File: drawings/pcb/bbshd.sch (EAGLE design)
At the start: 55 parts, among them IC1 LM358D

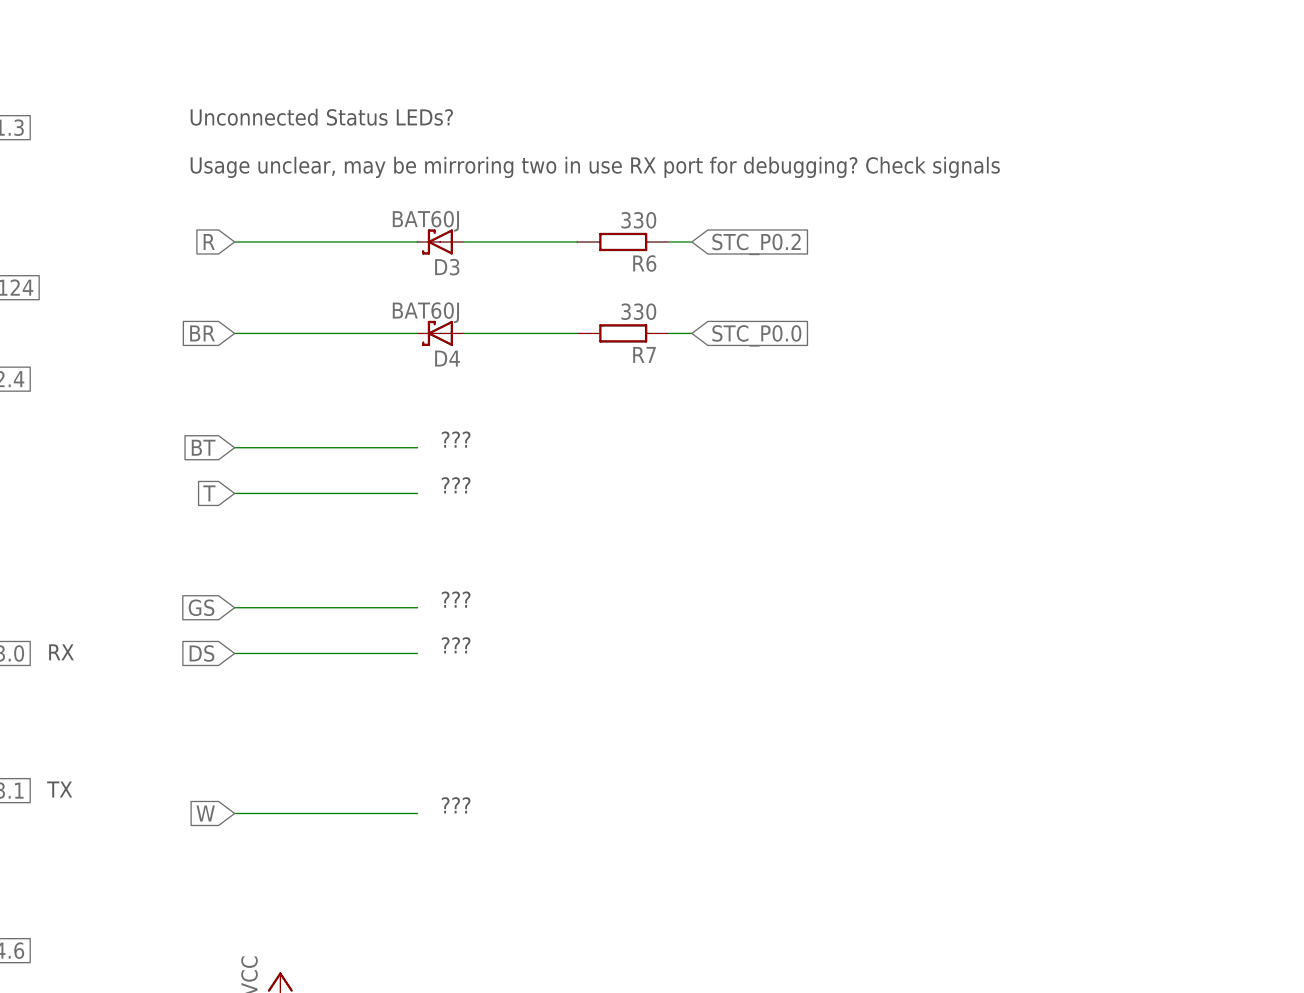
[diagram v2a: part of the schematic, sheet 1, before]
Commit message: Updated annotated photos with more info. Added info about additional UARTs brought out to pinheaders in schematic. Added template firmware src project, visual studio project files and makefile for SDCC compiler.
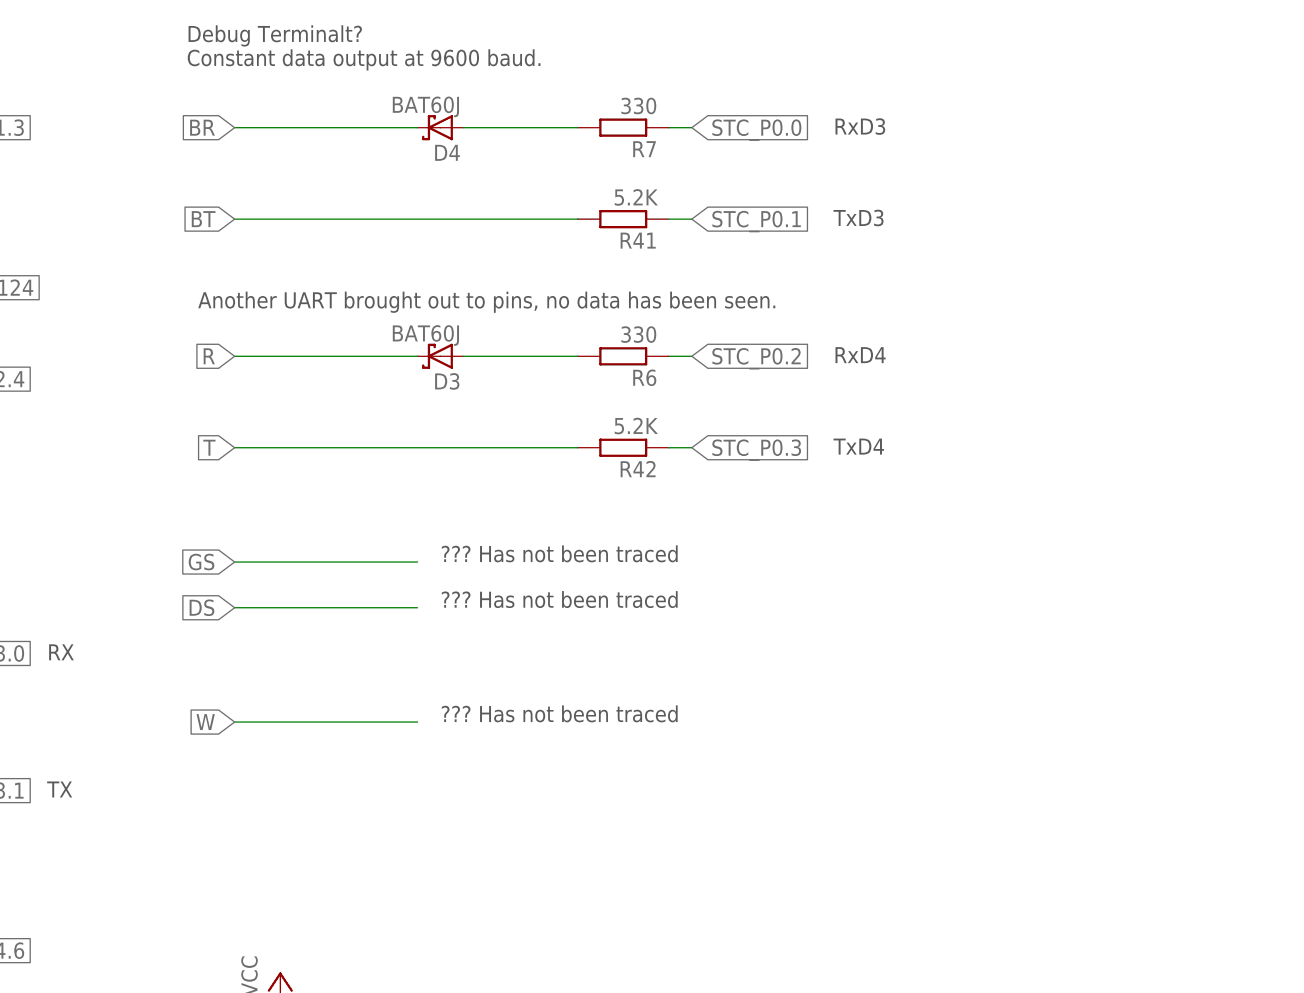
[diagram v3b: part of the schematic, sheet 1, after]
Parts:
- added R41, R42: 5.2K, rcl:R-EU_R0603
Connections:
- new net BT: R41.2
- new net STC_P0.1: R41.1
- new net STC_P0.3: R42.1
- new net T: R42.2
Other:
- note added: "??? Has not been traced"
- note added: "Another UART brought out to pins, no data has been seen."
- note added: "Debug Terminalt? Constant data output at 9600 baud."
- note added: "RxD3"
- note added: "RxD4"
- note added: "TxD3"
- note added: "TxD4"
- note removed: "???"
- note removed: "Unconnected Status LEDs? Usage unclear, may be mirroring two in use RX port for debugging? Check signals"
- moved on the sheet: D3, D4, R6, R7
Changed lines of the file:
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@@
 <part name="R40" library="rcl" deviceset="R-EU_" device="R0603" value="5.6K"/>
 <part name="LED1" library="led" deviceset="LED" device=""/>
+<part name="R41" library="rcl" deviceset="R-EU_" device="R0603" value="5.2K"/>
+<part name="R42" library="rcl" deviceset="R-EU_" device="R0603" value="5.2K"/>
 </parts>
 <sheets>
@@
 <text x="17.78" y="123.698" size="1.778" layer="97">GND</text>
 <text x="19.558" y="121.158" size="1.778" layer="97">5V</text>
-<text x="160.02" y="154.94" size="1.778" layer="97">Unconnected Status LEDs?
-Usage unclear, may be mirroring two in use RX port for debugging? Check signals</text>
 <text x="144.272" y="100.838" size="1.778" layer="97">RX</text>
 <text x="144.272" y="85.598" size="1.778" layer="97">TX</text>
@@
 <text x="17.018" y="60.198" size="1.778" layer="97">PAS1</text>
 <text x="17.018" y="62.738" size="1.778" layer="97">PAS2</text>
-<text x="187.96" y="124.46" size="1.778" layer="97">???</text>
-<text x="187.96" y="119.38" size="1.778" layer="97">???</text>
-<text x="187.96" y="106.68" size="1.778" layer="97">???</text>
-<text x="187.96" y="101.6" size="1.778" layer="97">???</text>
-<text x="187.96" y="83.82" size="1.778" layer="97">???</text>
+<text x="159.766" y="166.878" size="1.778" layer="97">Debug Terminalt?
+Constant data output at 9600 baud.</text>
+<text x="187.96" y="111.76" size="1.778" layer="97">??? Has not been traced</text>
+<text x="187.96" y="106.68" size="1.778" layer="97">??? Has not been traced</text>
+<text x="187.96" y="93.98" size="1.778" layer="97">??? Has not been traced</text>
 <text x="18.796" y="29.718" size="1.778" layer="97">SPD</text>
 <text x="217.17" y="20.066" size="2.54" layer="94">Daniel Nilsson</text>
 <text x="180.34" y="55.88" size="1.778" layer="97">ADC6 - Battery voltage measurement</text>
+<text x="231.648" y="123.698" size="1.778" layer="97">TxD4</text>
+<text x="231.648" y="133.858" size="1.778" layer="97">RxD4</text>
+<text x="231.648" y="159.258" size="1.778" layer="97">RxD3</text>
+<text x="231.648" y="149.098" size="1.778" layer="97">TxD3</text>
+<text x="161.036" y="139.954" size="1.778" layer="97">Another UART brought out to pins, no data has been seen.</text>
 </plain>
 <instances>
@@
 <instance part="P+3" gate="1" x="86.36" y="119.38"/>
 <instance part="D2" gate="G$1" x="78.74" y="101.6" rot="R180"/>
-<instance part="D3" gate="G$1" x="187.96" y="147.32" rot="R180"/>
-<instance part="R6" gate="G$1" x="208.28" y="147.32" rot="R180"/>
-<instance part="R7" gate="G$1" x="208.28" y="137.16" rot="R180"/>
-<instance part="D4" gate="G$1" x="187.96" y="137.16" rot="R180"/>
+<instance part="D3" gate="G$1" x="187.96" y="134.62" rot="R180"/>
+<instance part="R6" gate="G$1" x="208.28" y="134.62" rot="R180"/>
+<instance part="R7" gate="G$1" x="208.28" y="160.02" rot="R180"/>
+<instance part="D4" gate="G$1" x="187.96" y="160.02" rot="R180"/>
 <instance part="R8" gate="G$1" x="55.88" y="93.98" rot="R270"/>
 <instance part="D5" gate="G$1" x="55.88" y="109.22" rot="R270"/>
@@
 <instance part="R29" gate="G$1" x="182.88" y="48.26"/>
 <instance part="R30" gate="G$1" x="195.58" y="48.26"/>
+<instance part="R41" gate="G$1" x="208.28" y="149.86" rot="R180"/>
+<instance part="R42" gate="G$1" x="208.28" y="124.46" rot="R180"/>
 </instances>
 <busses>
@@
 <segment>
 <pinref part="D3" gate="G$1" pin="A"/>
-<wire x1="190.5" y1="147.32" x2="203.2" y2="147.32" width="0.1524" layer="91"/>
+<wire x1="190.5" y1="134.62" x2="203.2" y2="134.62" width="0.1524" layer="91"/>
 <pinref part="R6" gate="G$1" pin="2"/>
 </segment>
@@
 <segment>
 <pinref part="R6" gate="G$1" pin="1"/>
-<wire x1="213.36" y1="147.32" x2="215.9" y2="147.32" width="0.1524" layer="91"/>
-<label x="215.9" y="147.32" size="1.778" layer="95" xref="yes"/>
+<wire x1="213.36" y1="134.62" x2="215.9" y2="134.62" width="0.1524" layer="91"/>
+<label x="215.9" y="134.62" size="1.778" layer="95" xref="yes"/>
 </segment>
 </net>
@@
 <segment>
 <pinref part="R7" gate="G$1" pin="1"/>
-<wire x1="213.36" y1="137.16" x2="215.9" y2="137.16" width="0.1524" layer="91"/>
-<label x="215.9" y="137.16" size="1.778" layer="95" xref="yes"/>
+<wire x1="213.36" y1="160.02" x2="215.9" y2="160.02" width="0.1524" layer="91"/>
+<label x="215.9" y="160.02" size="1.778" layer="95" xref="yes"/>
 </segment>
 </net>
@@
 <pinref part="R7" gate="G$1" pin="2"/>
 <pinref part="D4" gate="G$1" pin="A"/>
-<wire x1="203.2" y1="137.16" x2="190.5" y2="137.16" width="0.1524" layer="91"/>
+<wire x1="203.2" y1="160.02" x2="190.5" y2="160.02" width="0.1524" layer="91"/>
 </segment>
 </net>
@@
 <segment>
 <pinref part="D3" gate="G$1" pin="C"/>
-<wire x1="185.42" y1="147.32" x2="165.1" y2="147.32" width="0.1524" layer="91"/>
-<label x="165.1" y="147.32" size="1.778" layer="95" rot="R180" xref="yes"/>
+<wire x1="185.42" y1="134.62" x2="165.1" y2="134.62" width="0.1524" layer="91"/>
+<label x="165.1" y="134.62" size="1.778" layer="95" rot="R180" xref="yes"/>
 </segment>
 </net>
@@
 <segment>
 <pinref part="D4" gate="G$1" pin="C"/>
-<wire x1="185.42" y1="137.16" x2="165.1" y2="137.16" width="0.1524" layer="91"/>
-<label x="165.1" y="137.16" size="1.778" layer="95" rot="R180" xref="yes"/>
+<wire x1="185.42" y1="160.02" x2="165.1" y2="160.02" width="0.1524" layer="91"/>
+<label x="165.1" y="160.02" size="1.778" layer="95" rot="R180" xref="yes"/>
 </segment>
 </net>
@@
 <net name="BT" class="0">
 <segment>
-<wire x1="185.42" y1="124.46" x2="165.1" y2="124.46" width="0.1524" layer="91"/>
+<wire x1="203.2" y1="149.86" x2="165.1" y2="149.86" width="0.1524" layer="91"/>
+<label x="165.1" y="149.86" size="1.778" layer="95" rot="R180" xref="yes"/>
+<pinref part="R41" gate="G$1" pin="2"/>
+</segment>
+</net>
+<net name="T" class="0">
+<segment>
+<wire x1="203.2" y1="124.46" x2="165.1" y2="124.46" width="0.1524" layer="91"/>
 <label x="165.1" y="124.46" size="1.778" layer="95" rot="R180" xref="yes"/>
-</segment>
-</net>
-<net name="T" class="0">
-<segment>
-<wire x1="185.42" y1="119.38" x2="165.1" y2="119.38" width="0.1524" layer="91"/>
-<label x="165.1" y="119.38" size="1.778" layer="95" rot="R180" xref="yes"/>
+<pinref part="R42" gate="G$1" pin="2"/>
 </segment>
 </net>
 <net name="GS" class="0">
+<segment>
+<wire x1="185.42" y1="111.76" x2="165.1" y2="111.76" width="0.1524" layer="91"/>
+<label x="165.1" y="111.76" size="1.778" layer="95" rot="R180" xref="yes"/>
+</segment>
+</net>
+<net name="DS" class="0">
 <segment>
 <wire x1="185.42" y1="106.68" x2="165.1" y2="106.68" width="0.1524" layer="91"/>
@@
 </segment>
 </net>
-<net name="DS" class="0">
-<segment>
-<wire x1="185.42" y1="101.6" x2="165.1" y2="101.6" width="0.1524" layer="91"/>
-<label x="165.1" y="101.6" size="1.778" layer="95" rot="R180" xref="yes"/>
-</segment>
-</net>
 <net name="W" class="0">
 <segment>
-<wire x1="185.42" y1="83.82" x2="165.1" y2="83.82" width="0.1524" layer="91"/>
-<label x="165.1" y="83.82" size="1.778" layer="95" rot="R180" xref="yes"/>
+<wire x1="185.42" y1="93.98" x2="165.1" y2="93.98" width="0.1524" layer="91"/>
+<label x="165.1" y="93.98" size="1.778" layer="95" rot="R180" xref="yes"/>
 </segment>
 </net>
@@
 </segment>
 </net>
+<net name="STC_P0.1" class="0">
+<segment>
+<pinref part="R41" gate="G$1" pin="1"/>
+<wire x1="213.36" y1="149.86" x2="215.9" y2="149.86" width="0.1524" layer="91"/>
+<label x="215.9" y="149.86" size="1.778" layer="95" xref="yes"/>
+</segment>
+</net>
+<net name="STC_P0.3" class="0">
+<segment>
+<pinref part="R42" gate="G$1" pin="1"/>
+<wire x1="213.36" y1="124.46" x2="215.9" y2="124.46" width="0.1524" layer="91"/>
+<label x="215.9" y="124.46" size="1.778" layer="95" xref="yes"/>
+</segment>
+</net>

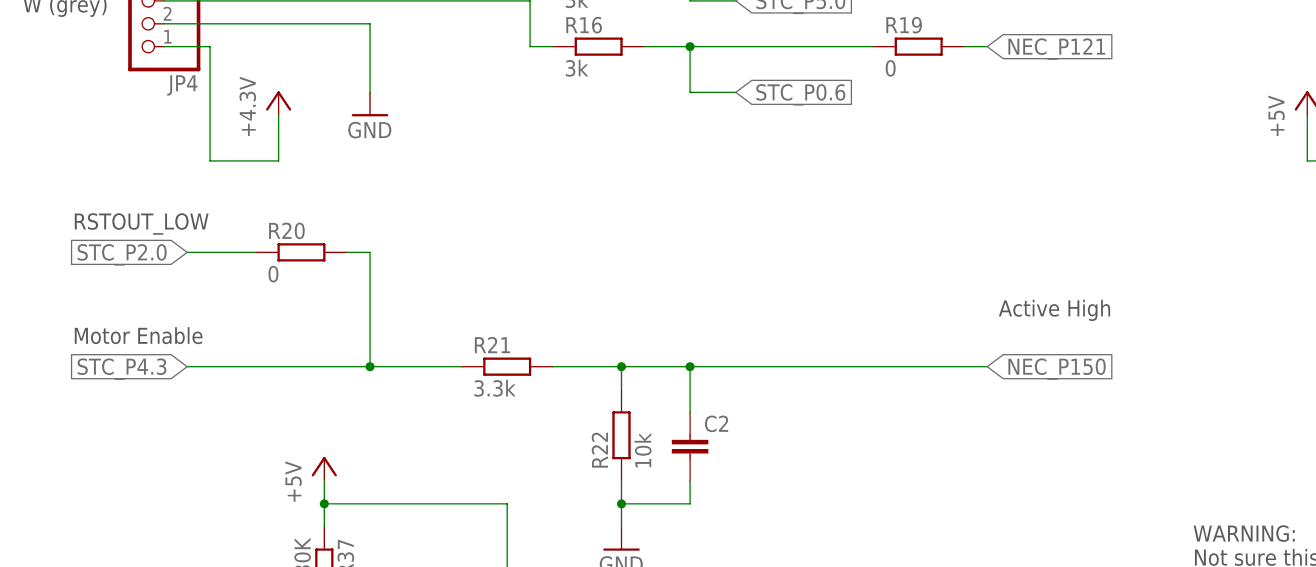
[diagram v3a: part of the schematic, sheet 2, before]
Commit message: Basic harware bring up in firmware. Successfully established communication with motor control MCU. Schematic corrections after new discoveries.
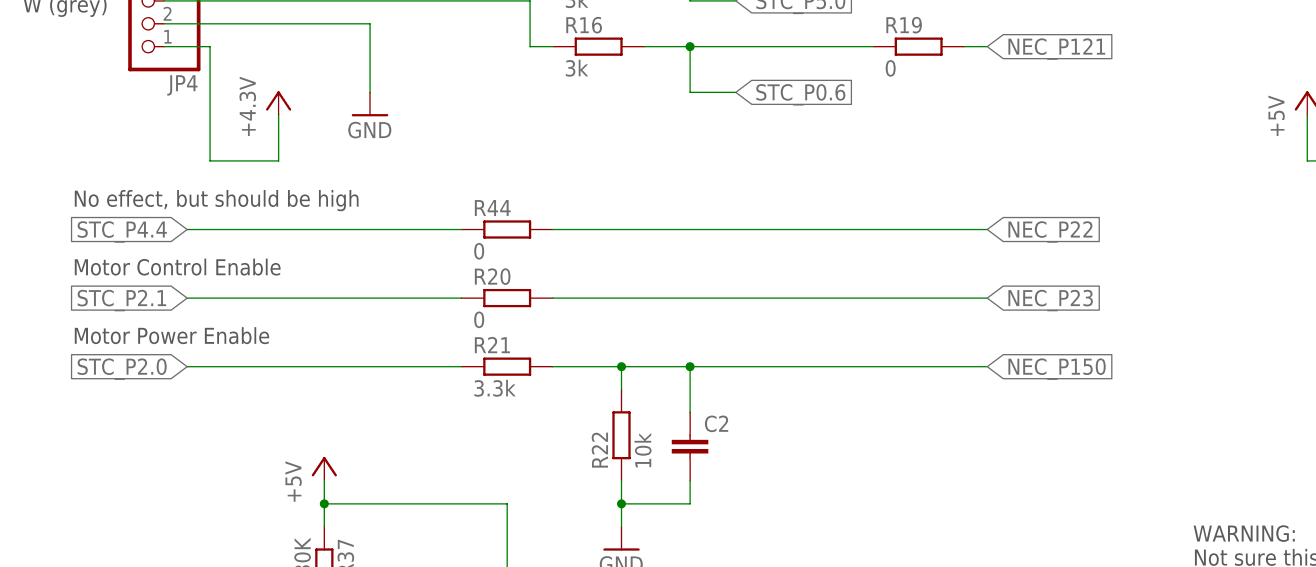
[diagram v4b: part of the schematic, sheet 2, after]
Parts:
- added R44: 0, rcl:R-EU_R0603
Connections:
- net STC_P2.0 renamed STC_P2.1
- removed net STC_P4.3: R20.2, R21.1
- new net NEC_P22: R44.2
- new net NEC_P23: R20.2
- new net STC_P4.4: R44.1
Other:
- note added: "Gear sensor"
- note added: "Motor Control Enable"
- note added: "Motor Power Enable"
- note added: "No effect, but should be high"
- note removed: "Active High"
- note removed: "Motor Enable"
- note removed: "RSTOUT_LOW"
- moved on the sheet: R20
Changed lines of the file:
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@@
 <part name="R18" library="rcl" deviceset="R-EU_" device="R0603" value="0"/>
 <part name="R19" library="rcl" deviceset="R-EU_" device="R0603" value="0"/>
-<part name="R20" library="rcl" deviceset="R-EU_" device="R0603" value="0"/>
 <part name="R21" library="rcl" deviceset="R-EU_" device="R0603" value="3.3k"/>
 <part name="R22" library="rcl" deviceset="R-EU_" device="R0603" value="10k"/>
@@
 <part name="R41" library="rcl" deviceset="R-EU_" device="R0603" value="5.2K"/>
 <part name="R42" library="rcl" deviceset="R-EU_" device="R0603" value="5.2K"/>
+<part name="R20" library="rcl" deviceset="R-EU_" device="R0603" value="0"/>
+<part name="R44" library="rcl" deviceset="R-EU_" device="R0603" value="0"/>
 </parts>
 <sheets>
@@
 <text x="159.766" y="166.878" size="1.778" layer="97">Debug Terminalt?
 Constant data output at 9600 baud.</text>
-<text x="187.96" y="111.76" size="1.778" layer="97">??? Has not been traced</text>
+<text x="187.96" y="111.76" size="1.778" layer="97">Gear sensor</text>
 <text x="187.96" y="106.68" size="1.778" layer="97">??? Has not been traced</text>
 <text x="187.96" y="93.98" size="1.778" layer="97">??? Has not been traced</text>
@@
 <text x="13.208" y="141.732" size="1.778" layer="97">V (blue)</text>
 <text x="12.192" y="135.89" size="1.778" layer="97">W (grey)</text>
-<text x="17.78" y="99.06" size="1.778" layer="97">Motor Enable</text>
-<text x="17.78" y="111.76" size="1.778" layer="97">RSTOUT_LOW</text>
+<text x="17.78" y="99.06" size="1.778" layer="97">Motor Power Enable</text>
 <text x="220.98" y="154.432" size="1.778" layer="97">NEC TxD</text>
 <text x="151.638" y="154.178" size="1.778" layer="97">STC RxD2</text>
@@
 <text x="165.1" y="127" size="1.778" layer="97">Some form of status LED.
 Seems to be blinking during normal operation.</text>
-<text x="120.65" y="102.108" size="1.778" layer="97">Active High</text>
+<text x="17.78" y="106.68" size="1.778" layer="97">Motor Control Enable</text>
+<text x="17.78" y="114.3" size="1.778" layer="97">No effect, but should be high</text>
 </plain>
 <instances>
@@
 <instance part="R18" gate="G$1" x="111.76" y="142.24"/>
 <instance part="R19" gate="G$1" x="111.76" y="132.08"/>
-<instance part="R20" gate="G$1" x="43.18" y="109.22"/>
 <instance part="R21" gate="G$1" x="66.04" y="96.52"/>
 <instance part="R22" gate="G$1" x="78.74" y="88.9" rot="R90"/>
@@
 <instance part="R40" gate="G$1" x="193.04" y="119.38"/>
 <instance part="LED1" gate="G$1" x="165.1" y="119.38" rot="R90"/>
+<instance part="R20" gate="G$1" x="66.04" y="104.14"/>
+<instance part="R44" gate="G$1" x="66.04" y="111.76"/>
 </instances>
 <busses>
@@
 <net name="STC_P2.0" class="0">
 <segment>
-<wire x1="30.48" y1="109.22" x2="38.1" y2="109.22" width="0.1524" layer="91"/>
-<label x="30.48" y="109.22" size="1.778" layer="95" rot="R180" xref="yes"/>
-<pinref part="R20" gate="G$1" pin="1"/>
-</segment>
-</net>
-<net name="STC_P4.3" class="0">
-<segment>
+<wire x1="30.48" y1="96.52" x2="60.96" y2="96.52" width="0.1524" layer="91"/>
 <label x="30.48" y="96.52" size="1.778" layer="95" rot="R180" xref="yes"/>
-<pinref part="R20" gate="G$1" pin="2"/>
-<wire x1="48.26" y1="109.22" x2="50.8" y2="109.22" width="0.1524" layer="91"/>
-<wire x1="50.8" y1="109.22" x2="50.8" y2="96.52" width="0.1524" layer="91"/>
-<wire x1="50.8" y1="96.52" x2="30.48" y2="96.52" width="0.1524" layer="91"/>
-<wire x1="50.8" y1="96.52" x2="60.96" y2="96.52" width="0.1524" layer="91"/>
-<junction x="50.8" y="96.52"/>
-<pinref part="R21" gate="G$1" pin="1"/>
 </segment>
 </net>
@@
 </segment>
 </net>
+<net name="STC_P2.1" class="0">
+<segment>
+<pinref part="R20" gate="G$1" pin="1"/>
+<wire x1="60.96" y1="104.14" x2="30.48" y2="104.14" width="0.1524" layer="91"/>
+<label x="30.48" y="104.14" size="1.778" layer="95" rot="R180" xref="yes"/>
+</segment>
+</net>
+<net name="NEC_P23" class="0">
+<segment>
+<pinref part="R20" gate="G$1" pin="2"/>
+<wire x1="71.12" y1="104.14" x2="119.38" y2="104.14" width="0.1524" layer="91"/>
+<label x="119.38" y="104.14" size="1.778" layer="95" xref="yes"/>
+</segment>
+</net>
+<net name="STC_P4.4" class="0">
+<segment>
+<pinref part="R44" gate="G$1" pin="1"/>
+<wire x1="60.96" y1="111.76" x2="30.48" y2="111.76" width="0.1524" layer="91"/>
+<label x="30.48" y="111.76" size="1.778" layer="95" rot="R180" xref="yes"/>
+</segment>
+</net>
+<net name="NEC_P22" class="0">
+<segment>
+<pinref part="R44" gate="G$1" pin="2"/>
+<wire x1="71.12" y1="111.76" x2="119.38" y2="111.76" width="0.1524" layer="91"/>
+<label x="119.38" y="111.76" size="1.778" layer="95" xref="yes"/>
+</segment>
+</net>
